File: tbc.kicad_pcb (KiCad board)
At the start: 2 copper layers, 0 parts

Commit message: added footprints for large ICs
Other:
- board outline added: 90.2 x 49.5 mm
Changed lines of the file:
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@@
   )
   (net 0 "")
+  (gr_rect (start 69.85 52.07) (end 160.02 101.6)
+    (stroke (width 0.1) (type default)) (fill none) (layer "Edge.Cuts"))
 )

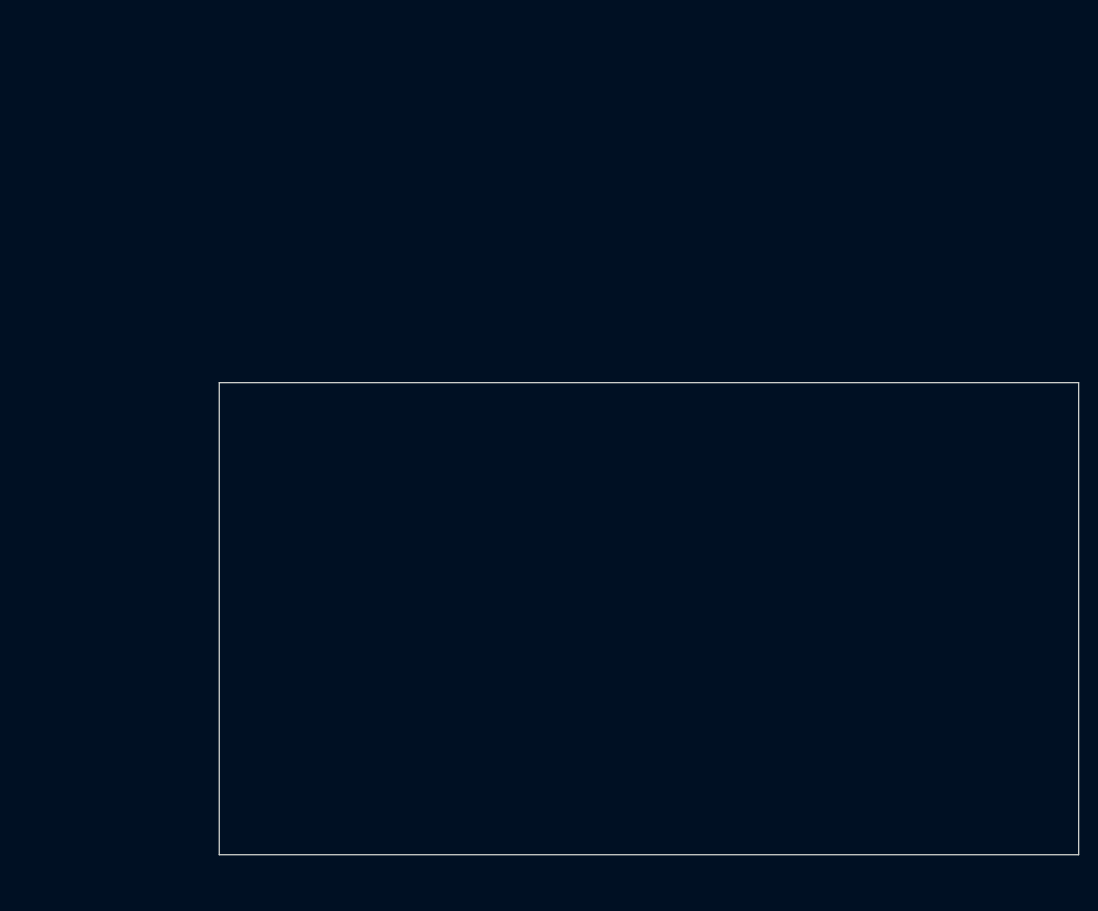
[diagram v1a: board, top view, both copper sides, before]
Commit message: resistor footprint added
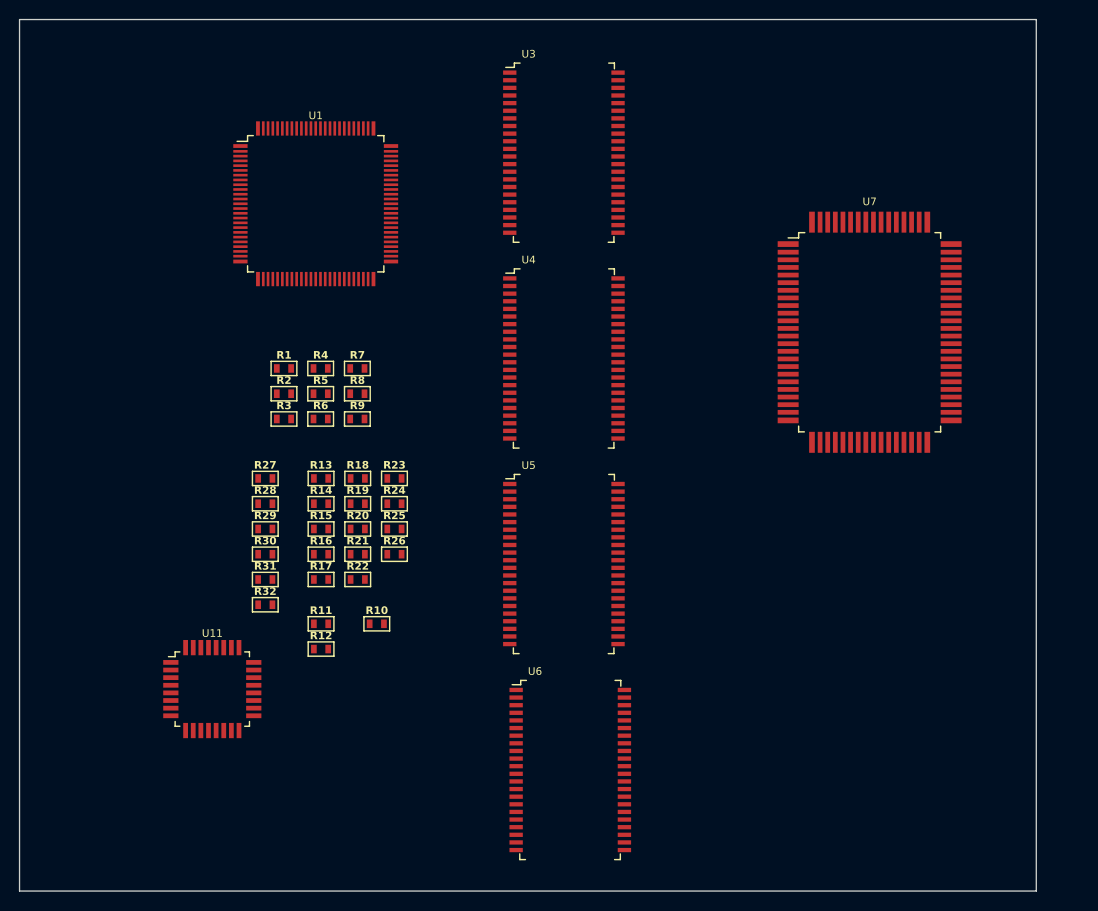
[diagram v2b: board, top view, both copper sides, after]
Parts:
- added R1: 18, tbc:R0603, F.Cu at (76.6, 50.6)
- added R10: 3K3, tbc:R0603, F.Cu at (86.4, 77.4)
- added R11: 2K2, tbc:R0603, F.Cu at (80.5, 77.4)
- added R12: 10k, tbc:R0603, F.Cu at (80.5, 80.0)
- added R13: 390, tbc:R0603, F.Cu at (80.5, 62.1)
- added R14: 2K2, tbc:R0603, F.Cu at (80.5, 64.8)
- added R15: 27, tbc:R0603, F.Cu at (80.5, 67.4)
- added R16: 75, tbc:R0603, F.Cu at (80.5, 70.1)
- added R17: 27, tbc:R0603, F.Cu at (80.5, 72.7)
- added R18: 75, tbc:R0603, F.Cu at (84.4, 62.1)
- added R19: 27, tbc:R0603, F.Cu at (84.4, 64.8)
- added R2: 18, tbc:R0603, F.Cu at (76.6, 53.2)
- added R20: 75, tbc:R0603, F.Cu at (84.4, 67.4)
- added R21: 8R2, tbc:R0603, F.Cu at (84.4, 70.1)
- added R22: 75, tbc:R0603, F.Cu at (84.4, 72.7)
- added R23: 13, tbc:R0603, F.Cu at (88.2, 62.1)
- added R24: 75, tbc:R0603, F.Cu at (88.2, 64.8)
- added R25: 13, tbc:R0603, F.Cu at (88.2, 67.4)
- added R26: 75, tbc:R0603, F.Cu at (88.2, 70.1)
- added R27: 10k, tbc:R0603, F.Cu at (74.7, 62.1)
- added R28: 4K7, tbc:R0603, F.Cu at (74.7, 64.8)
- added R29: 4K7, tbc:R0603, F.Cu at (74.7, 67.4)
- added R3: 18, tbc:R0603, F.Cu at (76.6, 55.9)
- added R30: 4K7, tbc:R0603, F.Cu at (74.7, 70.1)
- added R31: 4K7, tbc:R0603, F.Cu at (74.7, 72.7)
- added R32: 390, tbc:R0603, F.Cu at (74.7, 75.4)
- added R4: 18, tbc:R0603, F.Cu at (80.5, 50.6)
- added R5: 56, tbc:R0603, F.Cu at (80.5, 53.2)
- added R6: 56, tbc:R0603, F.Cu at (80.5, 55.9)
- added R7: 56, tbc:R0603, F.Cu at (84.3, 50.6)
- added R8: 56, tbc:R0603, F.Cu at (84.3, 53.2)
- added R9: 3K3, tbc:R0603, F.Cu at (84.3, 55.9)
- added U1: SAA7114H, tbc:LQFP100_14x14x1.4mm_Pitch0.5mm, F.Cu at (80.0, 33.3)
- added U11: STM32G051K8T6, tbc:QFP32_7x7x1.6mm_Pitch0.8mm, F.Cu at (69.1, 84.2)
- added U3: HM530281R, tbc:TTP-44DB, F.Cu at (106.0, 27.9)
- added U4: HM530281R, tbc:TTP-44DB, F.Cu at (106.0, 49.5)
- added U5: HM530281R, tbc:TTP-44DB, F.Cu at (106.0, 71.1)
- added U6: HM530281R, tbc:TTP-44DB, F.Cu at (106.7, 92.7)
- added U7: SAA7182A, tbc:QFP80_14x20x2.8mm_Pitch0.8mm, F.Cu at (138.1, 46.8)
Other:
- board size 90.2 x 49.5 mm -> 106.7 x 91.4 mm

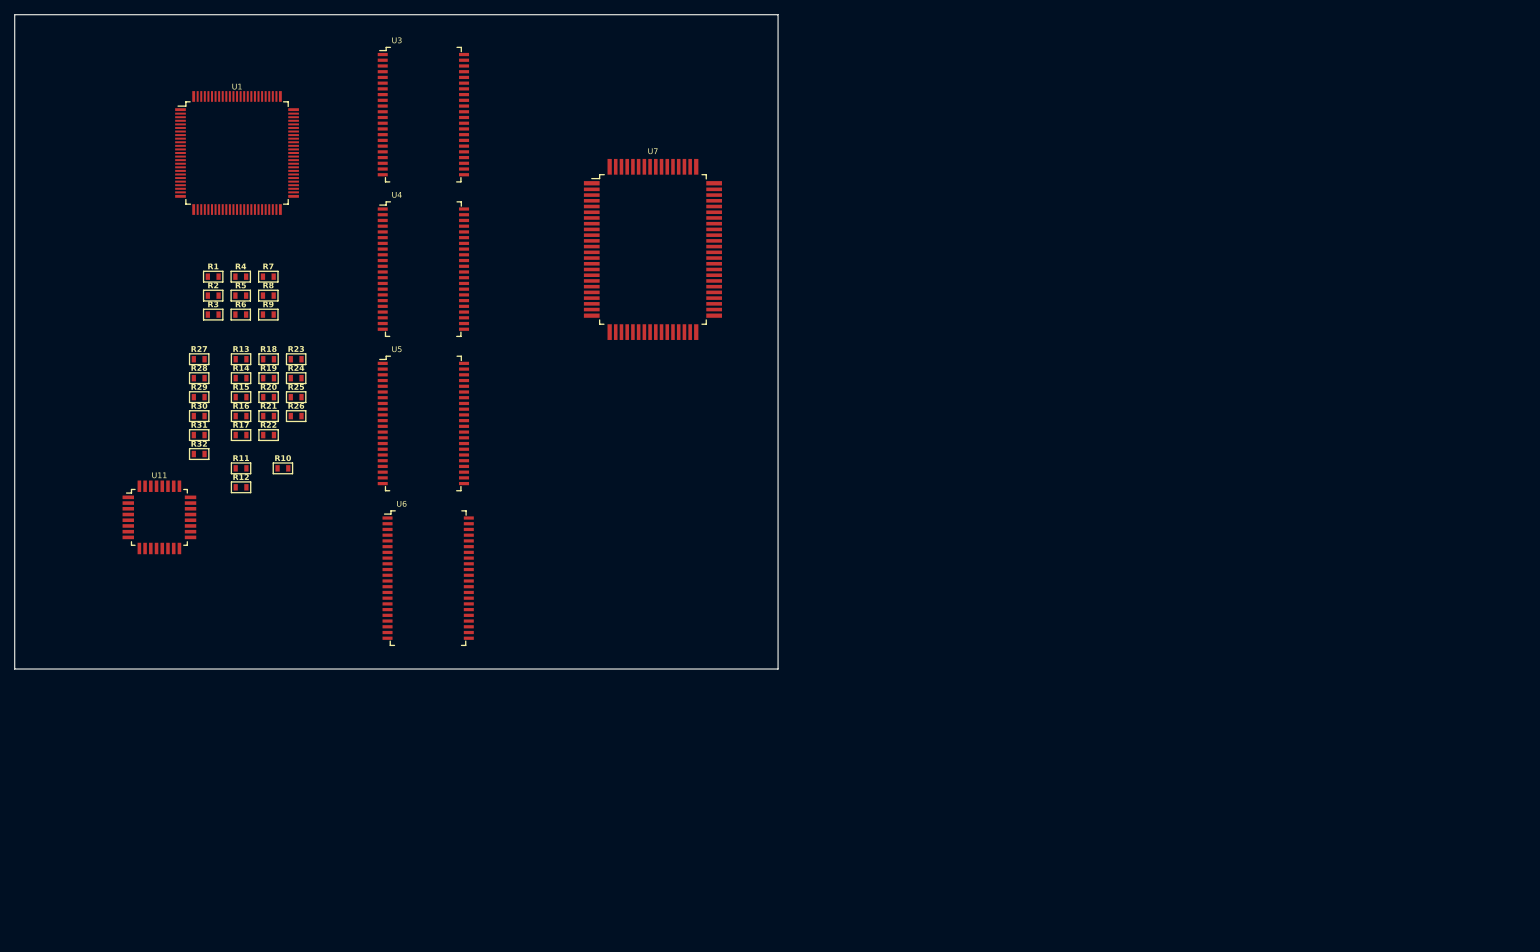
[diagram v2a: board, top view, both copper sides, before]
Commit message: added connector footprints
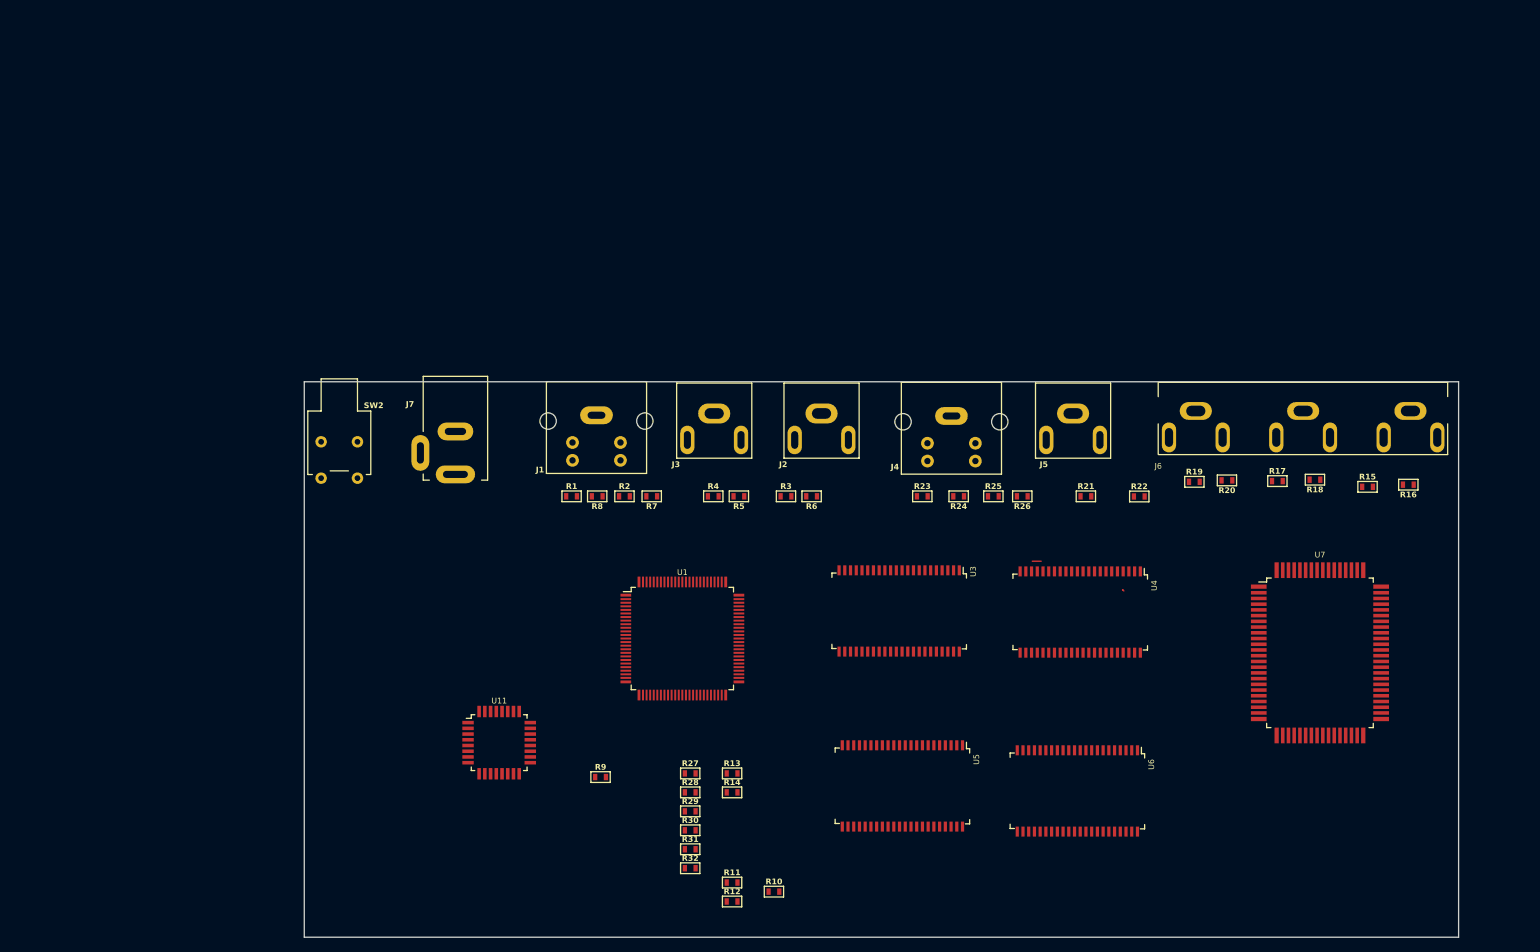
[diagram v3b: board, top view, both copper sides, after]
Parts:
- added J1: 5749181-1, tbc:5749181-1, F.Cu at (130.2, 70.0)
- added J2: PJRAN1X1U01X, tbc:PJRAN1X1U01X, F.Cu at (161.7, 69.7)
- added J3: PJRAN1X1U01X, tbc:PJRAN1X1U01X, F.Cu at (146.7, 69.7)
- added J4: 5749181-1, tbc:5749181-1, F.Cu at (179.8, 70.0)
- added J5: PJRAN1X1U01X, tbc:PJRAN1X1U01X, F.Cu at (196.8, 69.7)
- added J6: PJRAN3X1U03X, tbc:PJRAN3X1U03X, F.Cu at (228.9, 69.3)
- added J7: 4840.2201, tbc:4840.2201, F.Cu at (110.5, 72.2)
- added SW2: A11AH, tbc:A11AH, F.Cu at (94.3, 73.7)
- moved R16 163.4 mm to (243.7, 79.7), turned to 180 degrees
- moved R15 157.9 mm to (237.9, 80.0)
- moved R18 147.2 mm to (230.6, 79.0), turned to 180 degrees
- moved R17 145.0 mm to (225.3, 79.2)
- moved R20 134.4 mm to (218.3, 79.0), turned to 180 degrees
- moved R19 130.2 mm to (213.8, 79.2)
- moved R22 122.0 mm to (206.1, 81.3)
- moved R21 114.8 mm to (198.6, 81.3)
- moved U7 108.9 mm to (231.3, 103.2)
- moved U4 103.5 mm to (197.8, 97.5), turned to -90 degrees
- moved R26 102.1 mm to (189.7, 81.3), turned to 180 degrees
- moved R25 98.4 mm to (185.7, 81.3)
- moved U3 96.1 mm to (172.5, 97.3), turned to -90 degrees
- moved U6 95.5 mm to (197.4, 122.5), turned to -90 degrees
- moved R24 94.0 mm to (180.8, 81.3), turned to 180 degrees
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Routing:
- net /Frame Memories and Freeze/HPD0: track 0.00 -> 1.25 mm
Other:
- board size 106.7 x 91.4 mm -> 161.3 x 77.6 mm

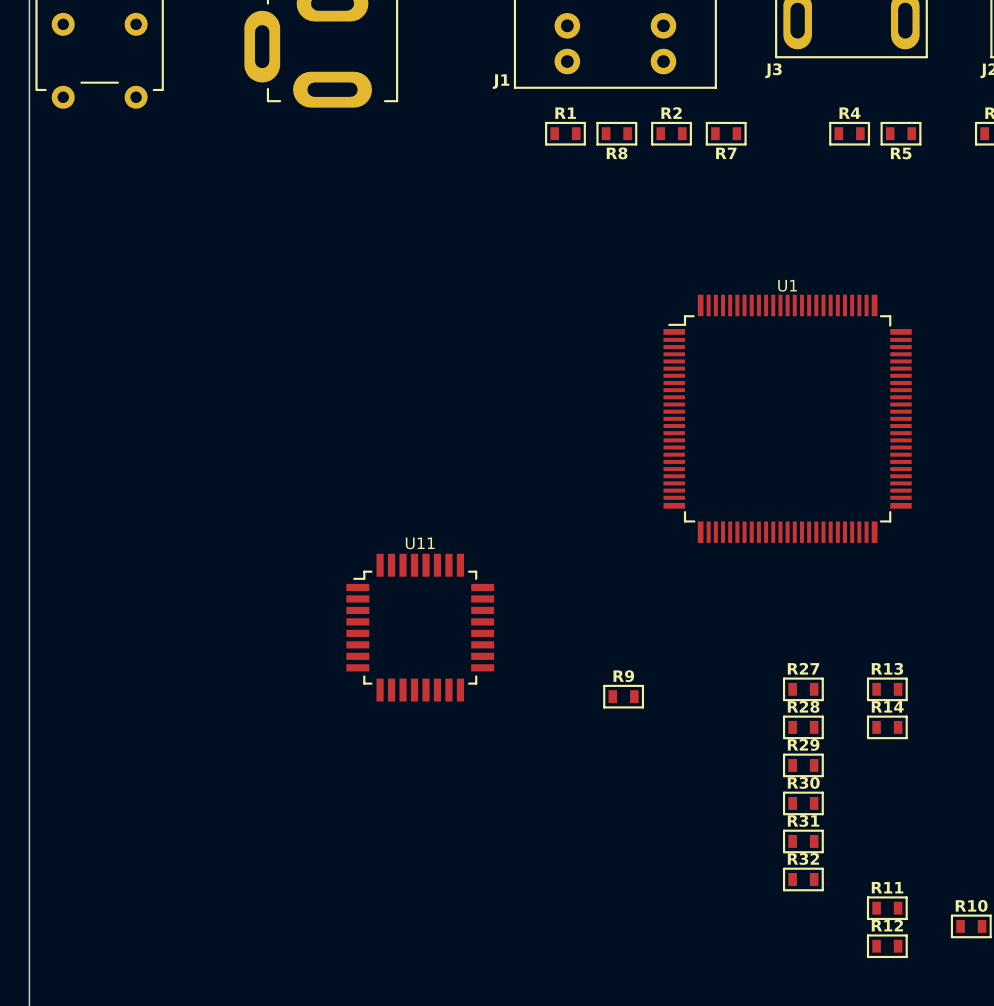
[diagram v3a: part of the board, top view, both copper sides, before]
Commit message: mosfet and tantalum footprints
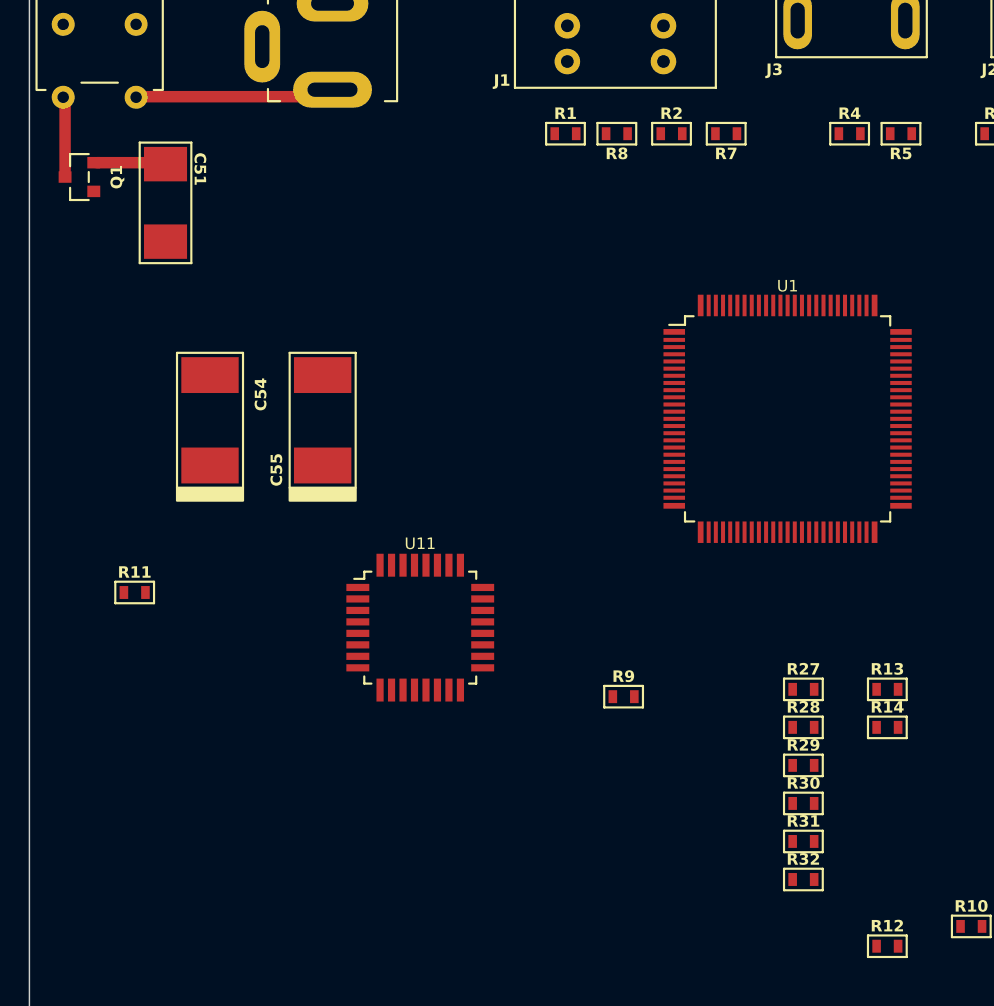
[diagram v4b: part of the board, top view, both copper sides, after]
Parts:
- added C51: 10uF|25V, tbc:293D_C, F.Cu at (98.8, 86.1)
- added C54: 22uF|25V, tbc:593D_D, F.Cu at (102.0, 101.2)
- added C55: 22uF|25V, tbc:593D_D, F.Cu at (109.8, 101.2)
- added Q1: BSS308PE, tbc:SOT23, F.Cu at (92.8, 84.3)
- moved R11 56.9 mm to (96.7, 113.2)
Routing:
- net Net-(SW2-A): track 0.00 -> 13.9 mm
- net Net-(Q1-D): track 0.00 -> 5.35 mm
- net Net-(Q1-S): track 0.00 -> 4.98 mm
